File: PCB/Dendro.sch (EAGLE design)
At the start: 5 parts

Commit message: Dendro PCB V1.1
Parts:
- NEOPIXEL: value 455-1750-1-ND -> (none)
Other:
- moved on the sheet: AS5311, BUTTON, NEOPIXEL, SHT30D

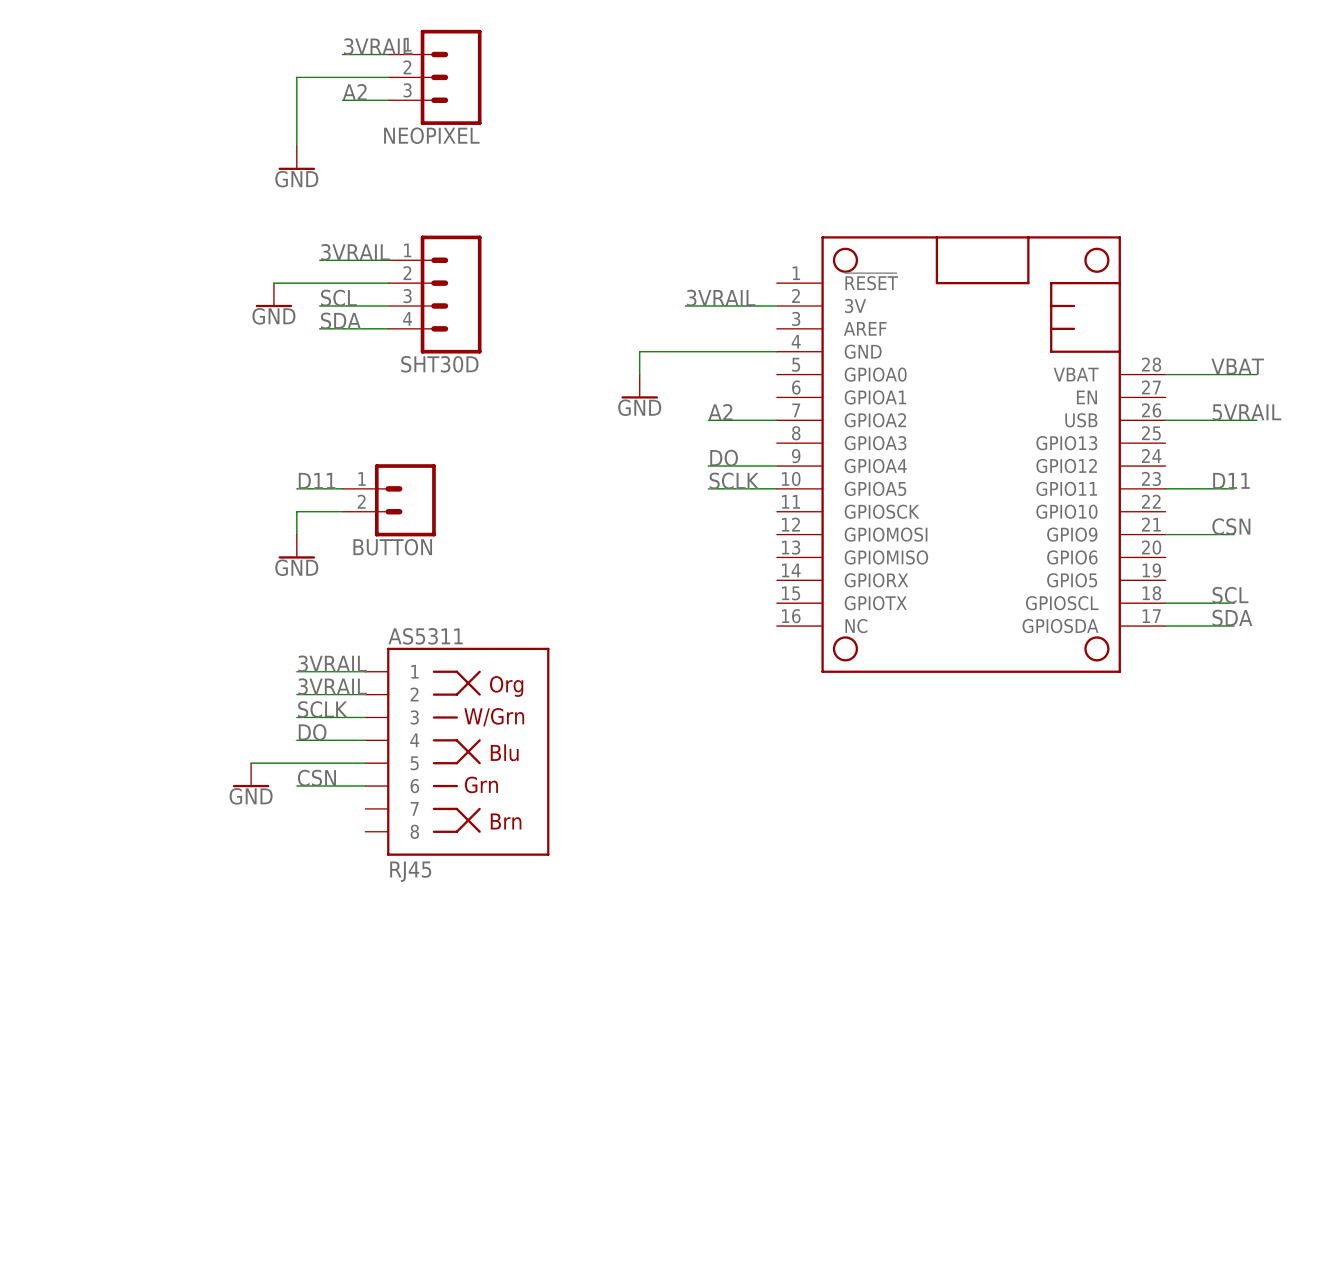
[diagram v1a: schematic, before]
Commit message: Updated code + PCB for summer deployments
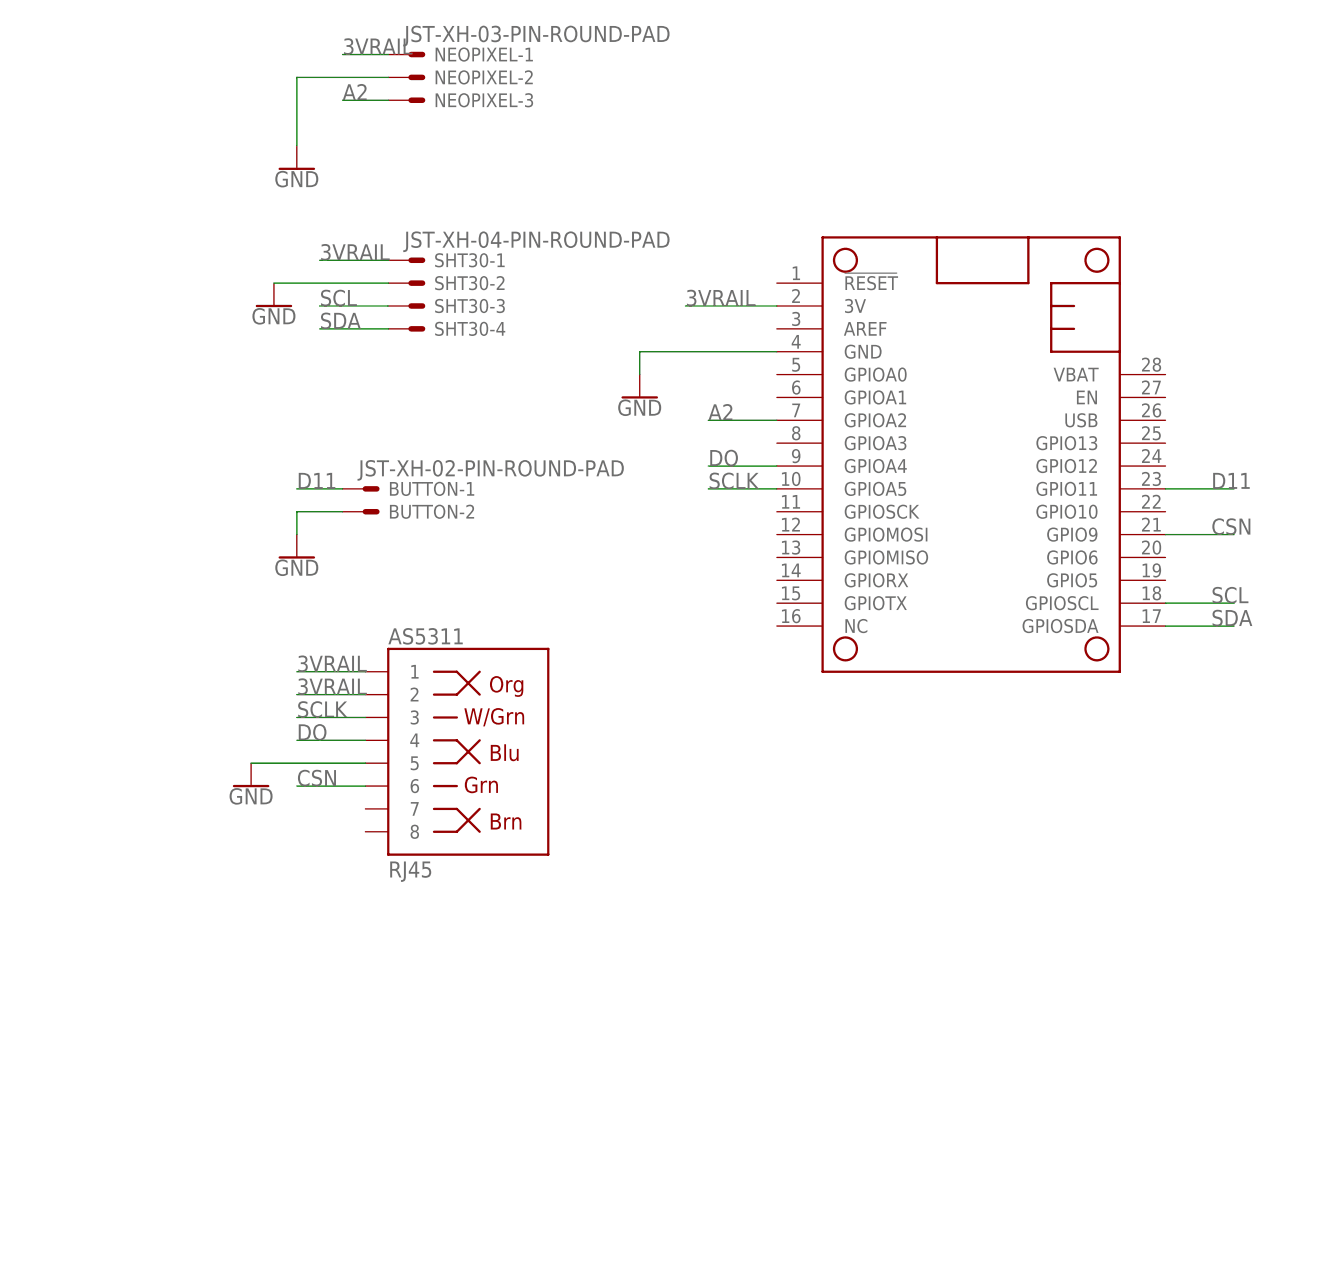
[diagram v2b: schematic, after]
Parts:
- removed SHT30D: (no value), SparkFun-Connectors:CONN_04
- added SHT30: JST-XH-04-PIN-ROUND-PAD, Rembrandt Electronics - JST XH Connectors v1-0:JST-XH-04-PIN-ROUND-PAD
- BUTTON: value (none) -> JST-XH-02-PIN-ROUND-PAD; device SparkFun-Connectors:CONN_02 -> Rembrandt Electronics - JST XH Connectors v1-0:JST-XH-02-PIN-ROUND-PAD
- NEOPIXEL: value (none) -> JST-XH-03-PIN-ROUND-PAD; device SparkFun-Connectors:CONN_03 -> Rembrandt Electronics - JST XH Connectors v1-0:JST-XH-03-PIN-ROUND-PAD
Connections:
- removed net 5VRAIL: MS1.USB
- removed net VBAT: MS1.VBAT
- net 3VRAIL: now also NEOPIXEL-1.S, SHT30-1.S; no longer NEOPIXEL.1, SHT30D.1
- net A2: now also NEOPIXEL-3.S; no longer NEOPIXEL.3
- net D11: now also BUTTON-1.S; no longer BUTTON.1
- net GND: now also BUTTON-2.S, NEOPIXEL-2.S, SHT30-2.S; no longer BUTTON.2, NEOPIXEL.2, SHT30D.2
- net SCL: now also SHT30-3.S; no longer SHT30D.3
- net SDA: now also SHT30-4.S; no longer SHT30D.4
